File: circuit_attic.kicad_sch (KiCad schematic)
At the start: 0 parts

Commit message: :sparkles: Add an op-amp mono-flop cirucuit
from https://github.com/moPsy-project/manual-gate-trigger-source
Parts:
- added C?: 22u, symbol Device:C_Polarized
- added D? (x2): 1N4148, symbol Device:D
- added R? (x2): 10k, symbol Device:R
- added R?: 470R, symbol Device:R
- added RV? (x2): 100k, symbol Device:R_Potentiometer
- added U?: TL072, symbol Amplifier_Operational:TL072
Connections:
- new net: C?.1, D?.2 (A), RV?.2, U?.6 (-)
- new net: D?.2 (A), R?.2, R?.2, U?.5 (+)
- new net: R?.1, RV?.1
- new net -12V: C?.2
- new net GND: D?.1 (K), R?.1
- new net TRIGGER_IN: D?.1 (K)
- new net TRIGGER_OUT: R?.1, R?.2, U?.7
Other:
- note added: "Consider an adjustable voltage divider here"
- note added: "Gate Length Selector"
- note added: "Mono Flop"
- note added: "Rather at voltage divider?"
- note added: "T = RC ln(1 + R2/R1) 7,1ms - 1,5s"
- note added: "https://github.com/moPsy-project/manual-gate-trigger-source/issues/9#issuecomment-1376312371"
- note added: "not retriggerable"

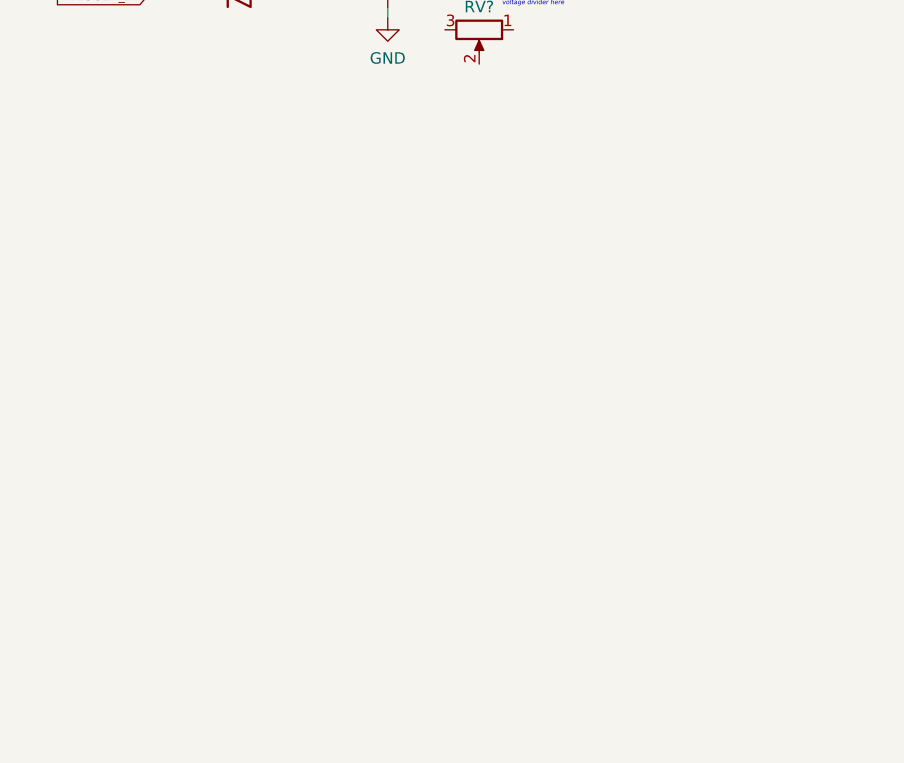
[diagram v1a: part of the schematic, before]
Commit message: :sparkles: Add a gate/trigger input
from https://github.com/moPsy-project/manual-gate-trigger-source
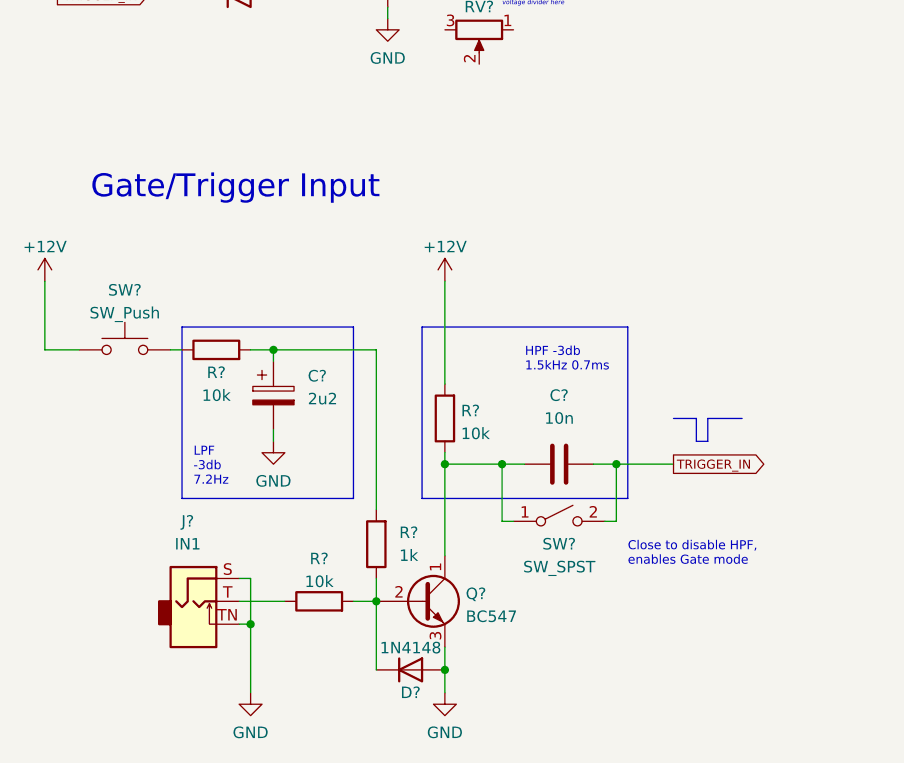
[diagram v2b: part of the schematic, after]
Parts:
- added C?: 2u2, symbol Device:C_Polarized
- added C?: 10n, symbol Device:C
- added D?: 1N4148, Diode_THT:D_DO-35_SOD27_P7.62mm_Horizontal, symbol Diode:1N4148
- added J?: IN1, Connector_Audio:Jack_3.5mm_QingPu_WQP-PJ398SM_Vertical_CircularHoles, symbol Connector:AudioJack2_Ground_SwitchT
- added Q?: BC547, Package_TO_SOT_THT:TO-92_Inline, symbol Transistor_BJT:BC547
- added R? (x3): 10k, symbol Device:R
- added R?: 1k, symbol Device:R
- added SW?: SW_SPST, symbol Switch:SW_SPST
- added SW?: SW_Push, symbol Switch:SW_Push
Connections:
- net GND: now also C?.2, D?.2 (A), J?.S, J?.TN, Q?.3 (E)
- net TRIGGER_IN: now also C?.2, SW?.2 (B)
- new net: C?.1, Q?.1 (C), R?.1, SW?.1 (A)
- new net: D?.1 (K), Q?.2 (B), R?.1, R?.2
- new net: R?.1, SW?.2
- new net: C?.1, R?.2, R?.2
- new net: J?.T, R?.1
- new net +12V: R?.2, SW?.1
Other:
- note added: "Close to disable HPF, enables Gate mode"
- note added: "Gate/Trigger Input"
- note added: "HPF -3db 1.5kHz 0.7ms"
- note added: "LPF -3db 7.2Hz"

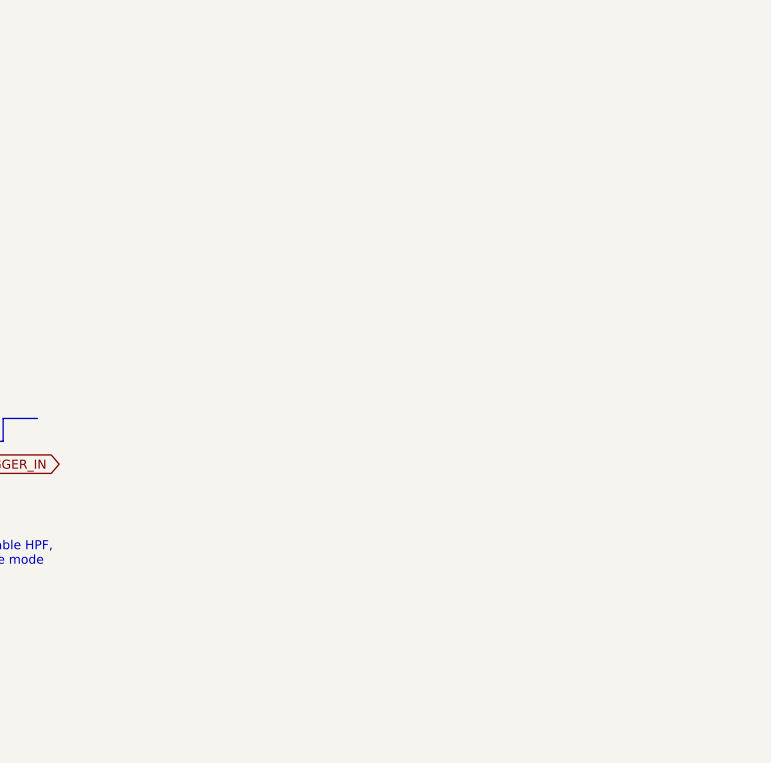
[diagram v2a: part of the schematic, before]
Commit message: :sparkles: Add a gate/trigger output
from https://github.com/moPsy-project/manual-gate-trigger-source
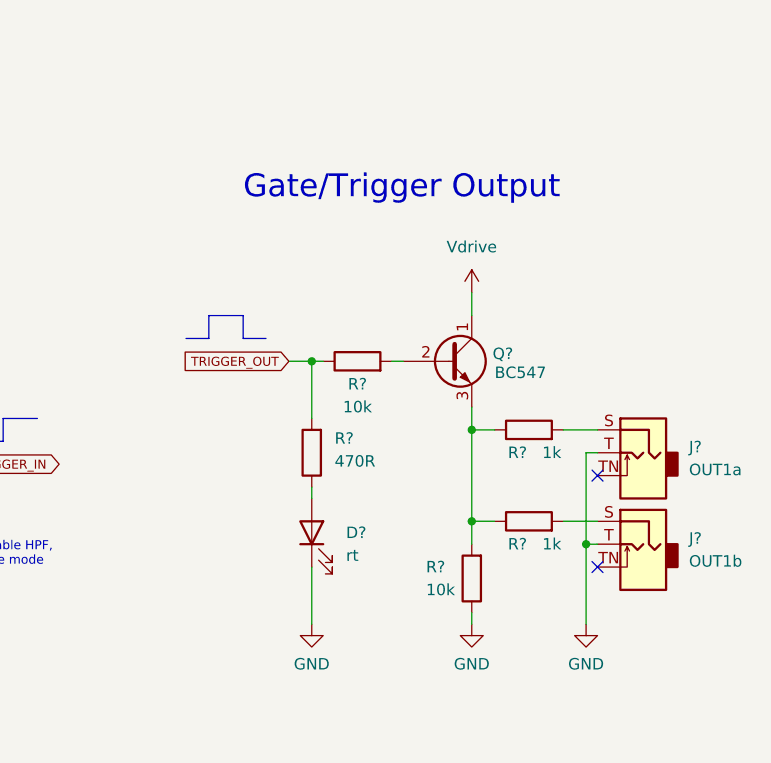
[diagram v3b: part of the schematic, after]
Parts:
- added D?: rt, symbol Device:LED
- added J?: OUT1b, Connector_Audio:Jack_3.5mm_QingPu_WQP-PJ398SM_Vertical_CircularHoles, symbol Connector:AudioJack2_Ground_SwitchT
- added J?: OUT1a, Connector_Audio:Jack_3.5mm_QingPu_WQP-PJ398SM_Vertical_CircularHoles, symbol Connector:AudioJack2_Ground_SwitchT
- added Q?: BC547, Package_TO_SOT_THT:TO-92_Inline, symbol Transistor_BJT:BC547
- added R? (x2): 10k, symbol Device:R
- added R? (x2): 1k, symbol Device:R
- added R?: 470R, symbol Device:R
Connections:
- net GND: now also D?.1 (K), J?.T, J?.T, R?.1
- net TRIGGER_OUT: now also R?.1, R?.2
- new net: Q?.2 (B), R?.2
- new net: Q?.3 (E), R?.1, R?.1, R?.2
- new net: J?.S, R?.2 (x2)
- new net: D?.2 (A), R?.1
- new net Vdrive: Q?.1 (C)
- no-connect marks 0 -> 2
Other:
- note added: "Gate/Trigger Output"

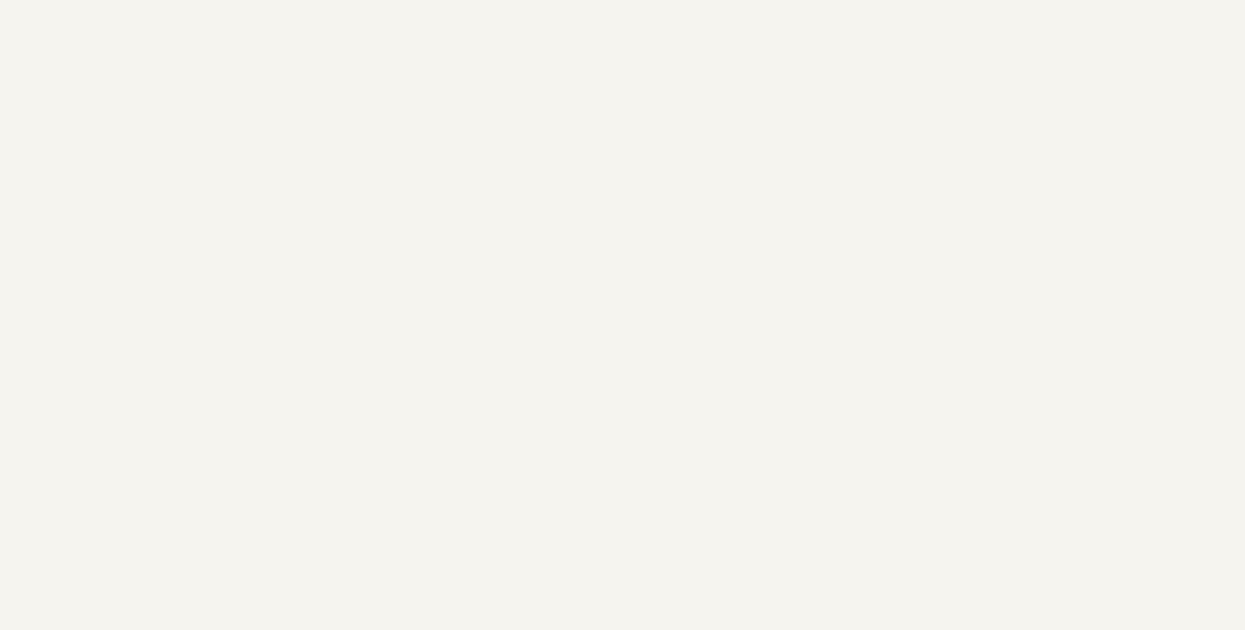
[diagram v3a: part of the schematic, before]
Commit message: :sparkles: Add transistor-based monoflop to circuit attic
This design does not work, but has been tried in
https://github.com/moPsy-project/moPsy-PSU/pull/16

Im saving it here for later.
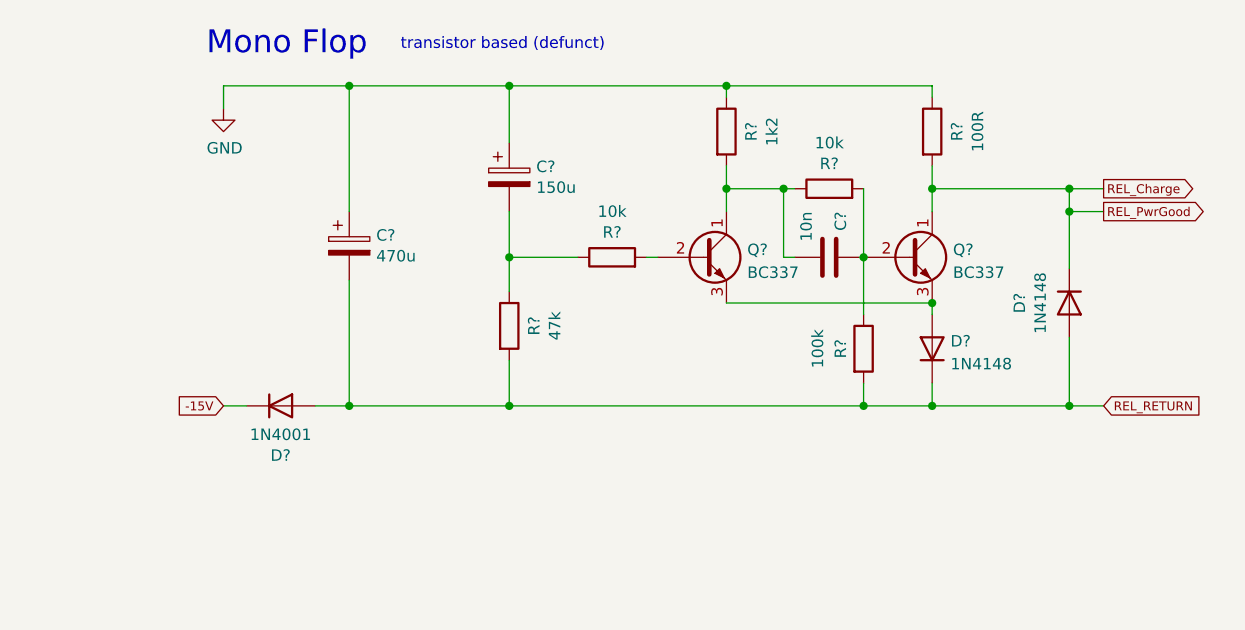
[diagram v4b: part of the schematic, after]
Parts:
- added C?: 10n, Capacitor_THT:C_Rect_L7.0mm_W2.5mm_P5.00mm, symbol Device:C
- added C?: 150u, Capacitor_THT:CP_Radial_D8.0mm_P3.50mm, symbol Device:CP
- added C?: 470u, Capacitor_THT:CP_Radial_D8.0mm_P3.50mm, symbol Device:CP
- added D?: 1N4148, Diode_THT:D_DO-41_SOD81_P7.62mm_Horizontal, symbol Device:D
- added D?: 1N4148, Diode_THT:D_DO-35_SOD27_P7.62mm_Horizontal, symbol Diode:1N4148
- added D?: 1N4001, Diode_THT:D_DO-41_SOD81_P7.62mm_Horizontal, symbol Device:D
- added Q? (x2): BC337, Package_TO_SOT_THT:TO-92_Inline, symbol Transistor_BJT:BC337
- added R? (x2): 10k, Resistor_THT:R_Axial_DIN0207_L6.3mm_D2.5mm_P7.62mm_Horizontal, symbol Device:R
- added R?: 47k, Resistor_THT:R_Axial_DIN0207_L6.3mm_D2.5mm_P7.62mm_Horizontal, symbol Device:R
- added R?: 100R, Resistor_THT:R_Axial_DIN0207_L6.3mm_D2.5mm_P7.62mm_Horizontal, symbol Device:R
- added R?: 1k2, Resistor_THT:R_Axial_DIN0207_L6.3mm_D2.5mm_P7.62mm_Horizontal, symbol Device:R
- added R?: 100k, Resistor_THT:R_Axial_DIN0207_L6.3mm_D2.5mm_P7.62mm_Horizontal, symbol Device:R
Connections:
- net GND: now also C?.1, C?.1, R?.1, R?.1
- new net: C?.1, Q?.2 (B), R?.1, R?.2
- new net: D?.2 (A), Q?.3 (E), Q?.3 (E)
- new net: C?.2, Q?.1 (C), R?.1, R?.2
- new net: C?.2, R?.1, R?.1
- new net: Q?.2 (B), R?.2
- new net -15V: D?.1 (K)
- new net REL_Charge: D?.1 (K), Q?.1 (C), R?.2
- new net REL_RETURN: C?.2, D?.1 (K), D?.2 (A), D?.2 (A), R?.2, R?.2
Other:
- note added: "transistor based (defunct)"
